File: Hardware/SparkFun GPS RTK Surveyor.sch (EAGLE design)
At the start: 98 parts, among them J2 CONN_04, J3 USB-C, J4 Qwiic Right Angle, J6 Start Base, J7 Power Switch, J9 CONN_04, Q2 MBT3904DW1T1, U1 MCP73831, U2 3.3V, U3 ZED-F9P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

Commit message: Production of v10
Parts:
- removed D9: BLUE, SparkFun-LED:LED-BLUE0603
- removed JP9: JUMPER-SMT_3_2-NC_TRACE_SILK, SparkFun-Jumpers:JUMPER-SMT_3_2-NC_TRACE_SILK
- removed R13: 1k, SparkFun-Resistors:1KOHM-0603-1/10W-1%
- removed R18, R19, R6: 33, SparkFun-Resistors:33OHM-0603-1/10W-1%
- removed R21, R22: 2.2k, SparkFun-Resistors:2.2KOHM-0603-1/10W-1%
- added C14: 10uF, SparkFun-Capacitors:10UF-0603-6.3V-20%
- added J11, J12, J13, J14: (no value), SparkFun-Connectors:CONN_041X04_NO_SILK_NO_POP
- added J15: (no value), SparkFun-Connectors:CONN_021X02_NO_SILK
- J1: device SparkFun-Connectors:CONN_08NO_SILK_DNP -> SparkFun-Connectors:CONN_041X04_NO_SILK_NO_POP
- R4: device SparkFun-Resistors:33OHM-0603-1/10W-1% -> SparkFun-Resistors:33OHM_RA-1206-1/16W-5%
- S1, S4: device SparkFun-Switches:MOMENTARY-SWITCH-SPST-SMD-6.0X3.5MM -> SparkFun-Switches:MOMENTARY-SWITCH-SPST-SMD-5.2-TALL-REDUNDANT
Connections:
- removed net !RESET: J1.6, R2D.2
- removed net !SAFE: J1.7, R2C.2
- removed net ATMEGA328_D10: R26.1
- removed net ATMEGA328_D13_SCK: R34.1
- removed net ATMEGA328_D2: J6.2
- removed net ATMEGA328_D6: R24.1
- removed net ATMEGA328_D9: R25.1
- removed net ESP32_IO12_MISO1: U5.MISO_H/IO12
- removed net ESP32_IO13_MOSI1: U5.MOSI_H/IO13
- removed net ESP32_IO15: U5.CS0_H/IO15
- removed net ESP32_IO2: U5.IO2
- removed net ESP32_IO4: U5.IO4
- removed net ESP32_IO5: R10.2, U5.CS0_V/IO5
- removed net EXTERNAL_SERIAL2_RXI: J9.3
- removed net EXTERNAL_SERIAL2_TXO: J9.2
- removed net N$14: R6.1, U3.RX2
- removed net N$19: R18.1, U3.RTK_STAT
- removed net N$20: R19.1, U3.GEO_STAT
- removed net N$23: D9.A, R10.1
- removed net N$7: D4.A, R13.1
- removed net SCL_PU1: JP9.1, R21.2
- removed net SDA_PU1: JP9.3, R22.2
- removed net SHLD: J3.SHLD
- removed net TX2_P: R4.1, U3.TX2
- new net !SAFE!: J13.2, R2C.2
- new net ESP32_12/BLUETOOTH_STATUS: R10.1, U5.MISO_H/IO12
- new net ESP32_13/POSACC1: R24.1, U5.MOSI_H/IO13
- new net ESP32_15/POSACC2: R25.1, U5.CS0_H/IO15
- new net ESP32_2/POSACC3: R26.1, U5.IO2
- new net ESP32_4/BASE_STAT: R34.1, U5.IO4
- new net ESP32_5/BASE_SELECT: J6.2, U5.CS0_V/IO5
- new net FENCE_LV: R4A.2, U3.GEO_STAT
- new net N$3: D4.A, R10.2
- new net RTK_LV: R4B.2, U3.RTK_STAT
- new net RX2_LV: R4C.2, U3.RX2
- new net TX2_LV: R4D.2, U3.TX2
- new net ZED_!RESET!: J13.3, R2D.2
- net 3.3V: now also C14.1, J1.4, J12.4, R12.2; no longer J1.1, JP9.2
- net 5V: now also J11.4, J7.2; no longer J7.1
- net ESP32_I34: now also J14.2
- net ESP32_I35: now also J14.1
- net ESP32_IO21_SDA: no longer R22.1
- net ESP32_IO22_SCL: no longer R21.1
- net ESP32_IO32: now also J14.4
- net ESP32_IO33: now also J14.3
- net EXTERNAL_SERIAL1_RXI: now also J12.2
- net EXTERNAL_SERIAL1_TXO: now also J12.3
- net FENCE_STAT: now also J1.2, R4A.1; no longer J1.5, R13.2, R19.2
- net GND: now also C14.2, J1.1, J11.1, J12.1, J3.SHLD; no longer D3.C, D9.C, J1.8
- net PPS_STAT: now also J13.1; no longer J1.3
- net RTK_STAT: now also D3.C, J1.3, R4B.1; no longer J1.4, R12.2, R18.2
- net TX_READY: now also J13.4; no longer J1.2
- net VBATT_SWTICHED: now also J7.1; no longer J7.2
- net ZED-RXI1: now also J15.2
- net ZED-RXI2: now also J11.2, J9.3, R4C.1; no longer R6.2
- net ZED-TXO1: now also J15.1
- net ZED-TXO2: now also J11.3, J9.2, R4D.1; no longer R4.2
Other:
- note added: "Bluetooth Status"
- note added: "Close DUAL_OUTPUT jumper to output NMEA Serial1 to both Bluetooth and external Serial1 port."
- note added: "RTK Solution: Off: None Blinking: Float Solid: Fixed"
- note added: "≤1000mm"
- note added: "≤100mm"
- note added: "≤20mm"
- note removed: "14.1mm RTK fix horz accuracy So no 1cm LED"
- note removed: "<100cm"
- note removed: "<10cm"
- note removed: "<1cm"
- note removed: "Close DUAL_OUTPUT jumper to output NMEA Serial1 to both Bluetooth and external Serial1 port. Warning: Jumper must be open if SERIAL1_CONNECTION is set to EXT CNTR and BLUETOOTH_BROADCAST is set to"
- note removed: "Flashing RTK at 2Hz is RTK Float Fix"
- note removed: "I2C Pull Ups"
- note removed: "Invert RTK LED"
- note removed: "PTH holes to a few GPIO on ATmega"
- note removed: "PTH holes to all primary signals (RX/TX1, RX/TX2, etc)"
- note removed: "RTK Fix: RTK LED turns off SW Map Icon turns green RTK Fix"
- moved on the sheet: BLUETOOTH_BROADCAST, BYP, C10, C11, C12, C13, C8, C9, D10, D11, D12, D15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

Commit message: Completed 4 layer design with 4pin SMD JST connectors
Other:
- note added: "Data Output Selection"
- note added: "RTK Solution: Off: None Blinking: Float On: Fixed"
- note added: "add microSD"
- note removed: "RTK Solution: Off: None Blinking: Float Solid: Fixed"
- moved on the sheet: BLUETOOTH_BROADCAST, BYP, C13, C14, C8, C9, D1, D15, D3, D5, D7, DUAL_OUTPUT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

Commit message: v11 add microSD. Fix power switch. Fix BT switch. Add I2C. Remove old files. Add enclsoure cut files.
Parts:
- removed BYP: JUMPER-SMT_2_NO_SILK, SparkFun-Jumpers:JUMPER-SMT_2_NO_SILK
- removed D15: Yellow, SparkFun-LED:LED-YELLOW0603
- removed F1: 6V/2A, SparkFun-Fuses:PPTC_6V2A
- removed LED1: GREEN, SparkFun-LED:LED-GREEN0603
- removed R33: 1k, SparkFun-Resistors:1KOHM-0603-1/10W-1%
- removed R36: 330, SparkFun-Resistors:330OHM-0603-1/10W-1%
- added C16: 0.1uF, SparkFun-Capacitors:0.1UF-0603-25V-(+80/-20%)
- added D9: 3A/10V/280mV, SparkFun-DiscreteSemi:DIODE-SCHOTTKY-BAT60A
- added J17: MICRO-SD, SparkFun-Connectors:MICRO-SD_CARD_SOCKETPUSH-PUSH
- added R13: 100k, SparkFun-Resistors:100KOHM-0603-1/10W-1%
- D10, D11, D8: value BLUE -> GREEN; device SparkFun-LED:LED-BLUE0603 -> SparkFun-LED:LED-GREEN0603
- D12: value BLUE -> RED; device SparkFun-LED:LED-BLUE0603 -> SparkFun-LED:LED-RED0603
- D3: value GREEN -> WHITE; device SparkFun-LED:LED-GREEN0603 -> SparkFun-LED:LED-WHITE0603
- R7: value 2.2k -> 1k; device SparkFun-Resistors:2.2KOHM-0603-1/10W-1% -> SparkFun-Resistors:1KOHM-0603-1/10W-1%
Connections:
- net ESP32_13/POSACC1 renamed ESP32_13/POSACC3
- net ESP32_2/POSACC3 renamed ESP32_2/POSACC1
- removed net ESP32_IO21_SDA: U5.IO21
- removed net ESP32_IO22_SCL: U5.IO22
- removed net ESP32_IO25: U5.IO25
- removed net ESP32_IO26: U5.IO26
- removed net ESP32_IO27: U5.IO27
- removed net N$28: LED1.A, R36.1
- removed net N$31: D15.A, R33.1
- removed net TX_READY: J13.4, R9A.2
- removed net VBATT_SWTICHED: D7.C, J7.1
- removed net ZED_!RESET!: J13.3, R2D.2
- new net ESP32_IO25/!CS!: J17.CS, R13.1, U5.IO25
- new net ESP32_IO26/TX_READY: J13.4, R9A.2, U5.IO26
- new net ESP32_IO27/ZED-!RESET!: J13.3, R2D.2, U5.IO27
- new net VIN: C9.1, D5.A, D6.5, D7.C, D9.C, J5.VBUS, J7.1, U1.VIN
- net 3.3V: now also C16.1, J17.VCC, R13.2; no longer R33.2, R36.2
- net 5V: no longer BYP.2, C9.1, D5.A, D6.5, F1.2, J5.VBUS, U1.VIN
- net ESP32_IO18_SCK0: now also J17.SCK
- net ESP32_IO19_MISO0: now also J17.DO
- net ESP32_IO23_MOSI0: now also J17.DI
- net ESP32_RXI: no longer D15.C
- net ESP32_TXO: no longer LED1.C
- net GND: now also C16.2, J17.GND, J17.SHIELD
- net N$32: now also D9.A; no longer BYP.1, F1.1
- net SCL: now also U5.IO22
- net SDA: now also U5.IO21
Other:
- note added: "5V is not guaranteed May be 3.5-5V"
- note added: "Charge current: 1000mA (1000V/Rprog)"
- note added: "USB-to-Serial For ESP32"
- note added: "μSD"
- note removed: "Charge current: 450mA (1000V/Rprog)"
- note removed: "This is the bypass jumper Close only if you know what you're doing."
- note removed: "USB-to-Serial"
- note removed: "add microSD"
- moved on the sheet: C4, C5, C6, C8, C9, D5, D6, D7, J10, J13, J15, J5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

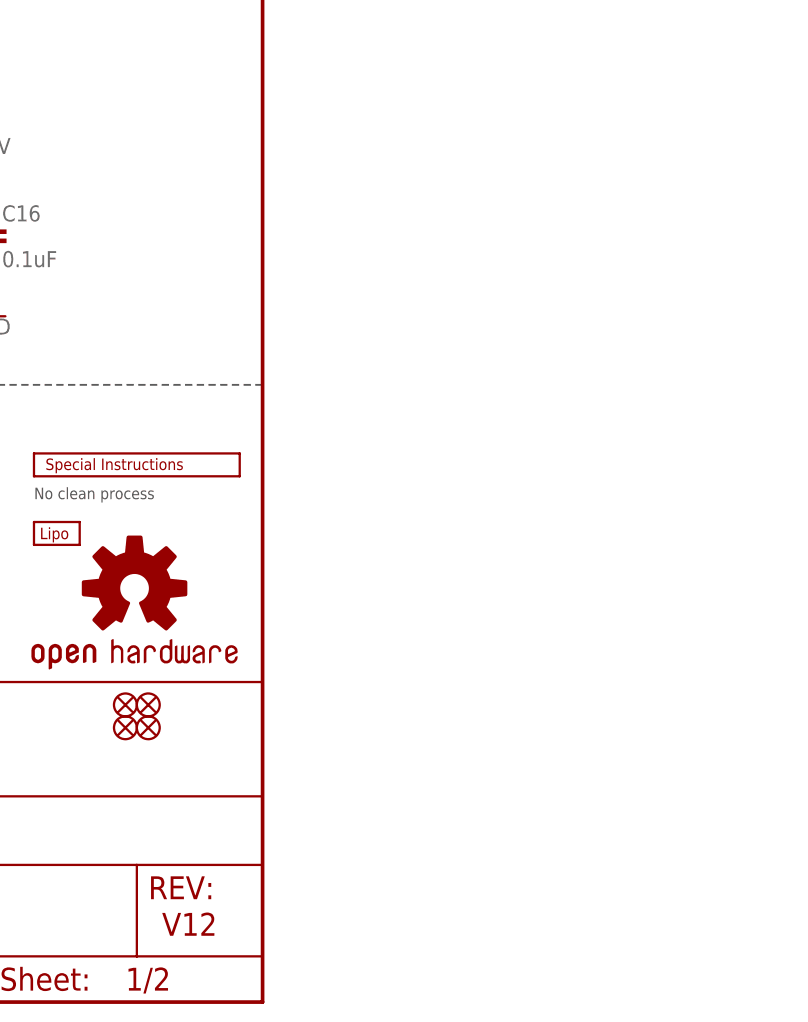
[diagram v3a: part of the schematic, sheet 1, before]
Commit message: Change LED colors.
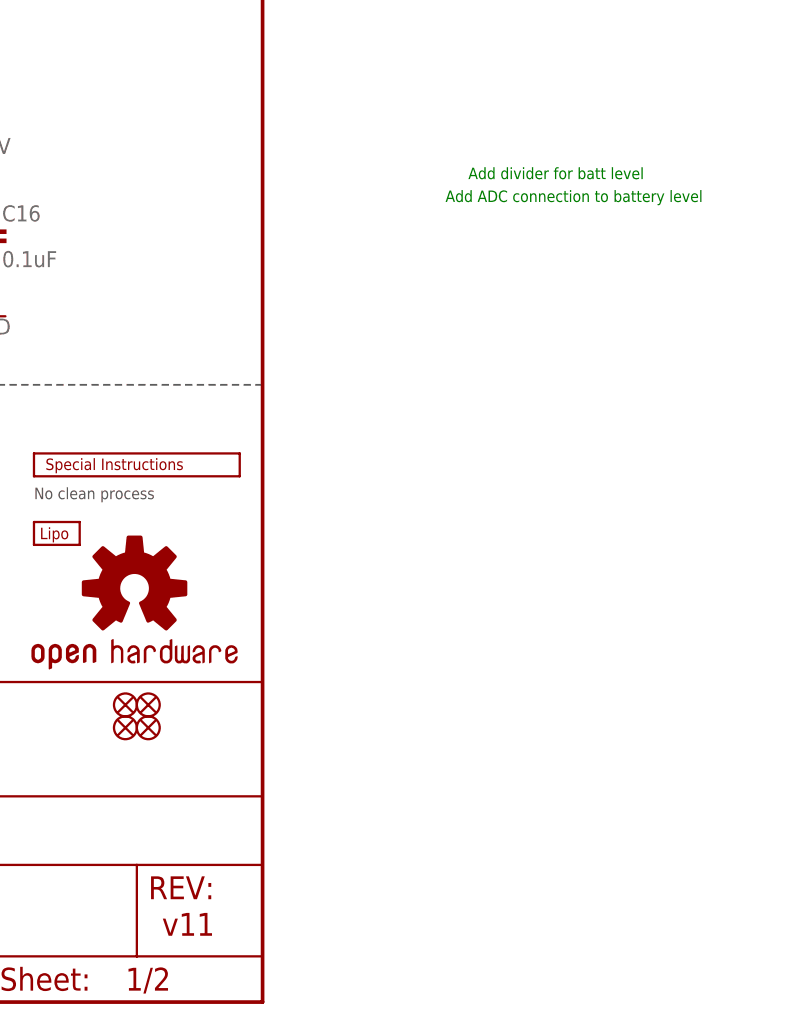
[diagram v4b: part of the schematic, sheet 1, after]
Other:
- note added: "Add ADC connection to battery level"
- note added: "Add divider for batt level"
- note added: "v11"
- note removed: "V12"
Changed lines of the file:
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@@
 <?xml version="1.0" encoding="utf-8"?>
 <!DOCTYPE eagle SYSTEM "eagle.dtd">
-<eagle version="9.6.0">
+<eagle version="9.6.2">
 <drawing>
 <settings>
@@
 <sheet>
 <plain>
-<text x="420.624" y="7.366" size="2.54" layer="94">V12</text>
+<text x="420.624" y="7.366" size="2.54" layer="94">v11</text>
 <text x="93.98" y="187.96" size="1.778" layer="97" align="center">7-bit unshifted I2C address: 0x42</text>
 <text x="89.662" y="262.382" size="2.54" layer="94" rot="MR180" align="center">Ublox ZED-F9P</text>
@@
 <text x="104.14" y="30.48" size="1.27" layer="97" align="center">5V is not guaranteed
 May be 3.5-5V</text>
+<text x="454.66" y="91.44" size="1.27" layer="91">Add divider for batt level</text>
+<text x="452.12" y="88.9" size="1.27" layer="91">Add ADC connection to battery level</text>
 </plain>
 <instances>

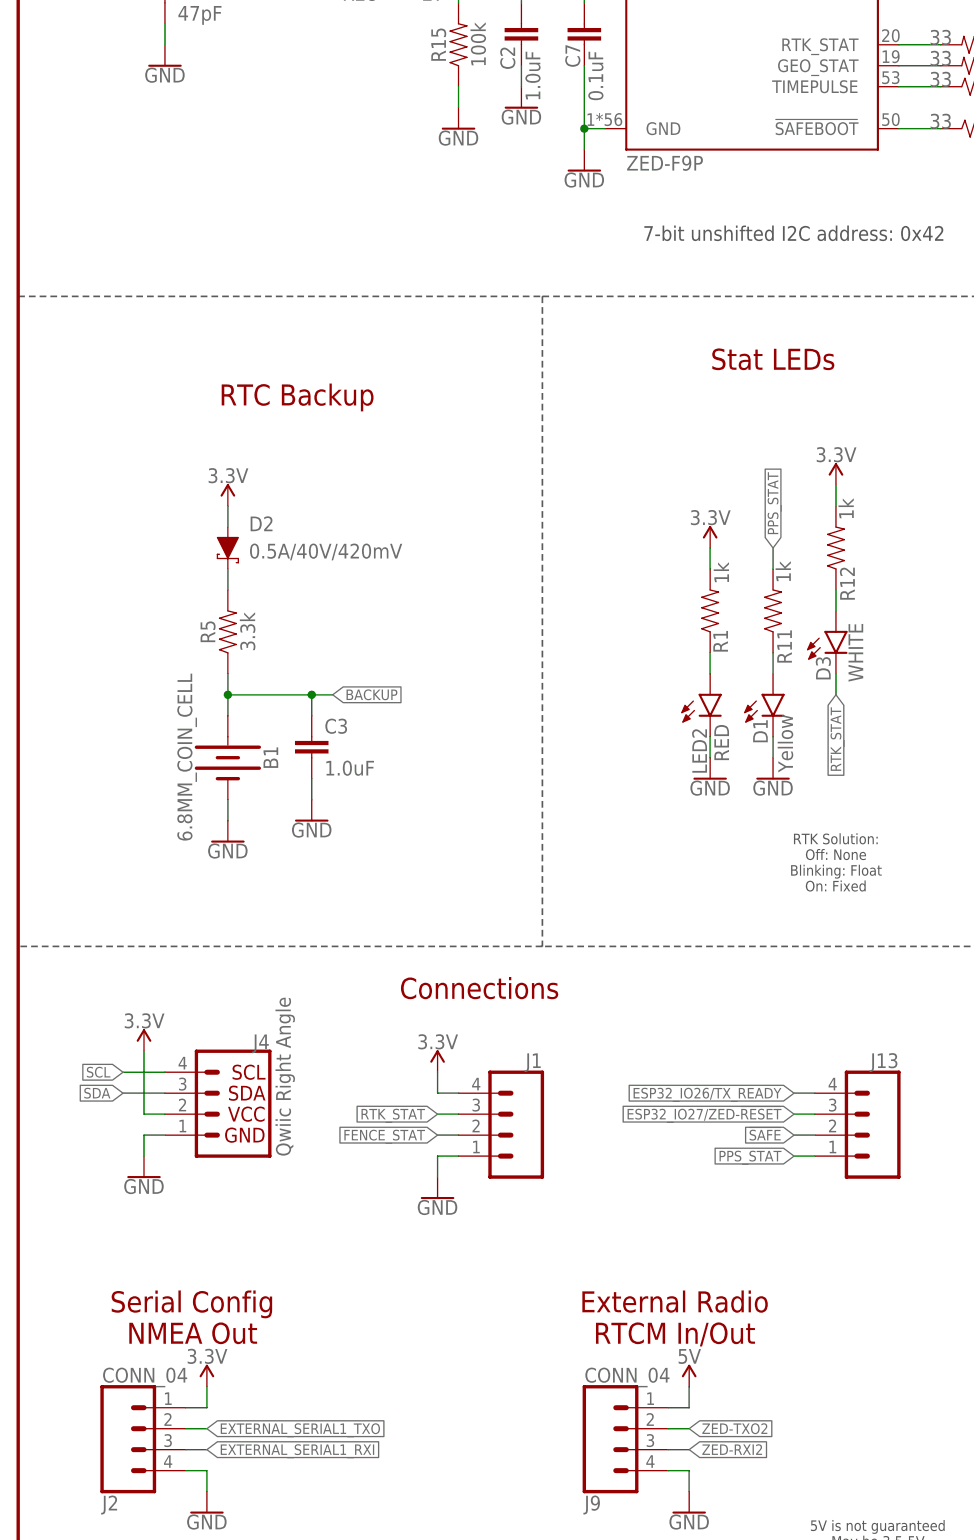
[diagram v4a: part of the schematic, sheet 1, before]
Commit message: Update parts with prod_ids
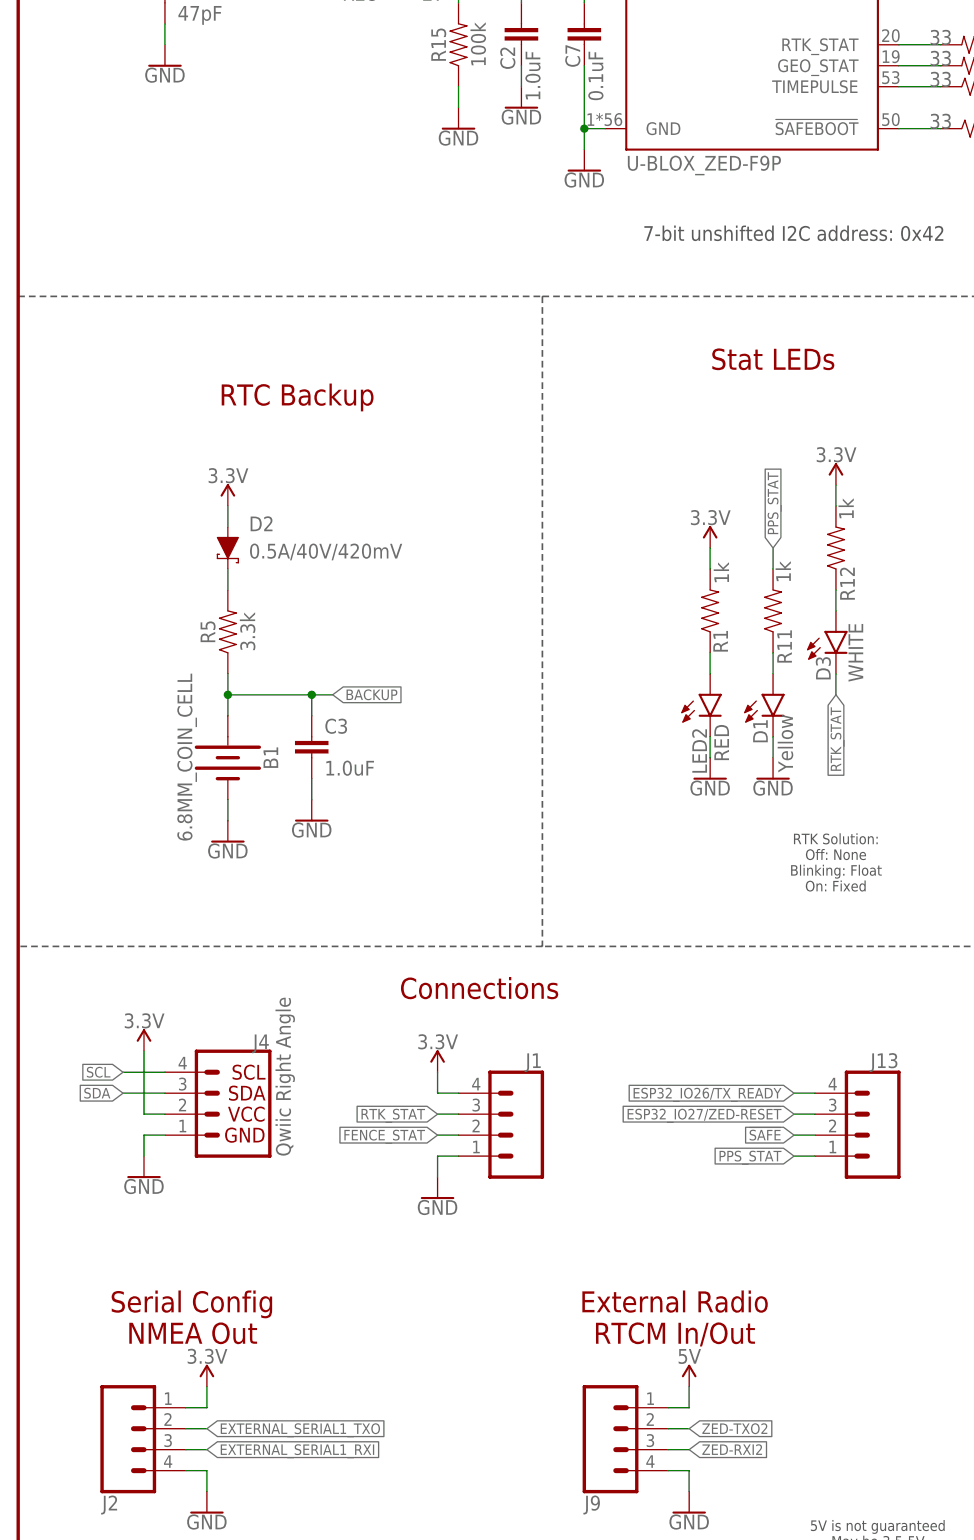
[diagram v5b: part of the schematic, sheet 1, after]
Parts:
- J2, J9: value CONN_04 -> (none); device SparkFun GPS RTK Surveyor:CONN_04 -> SparkFun-Connectors:CONN_04JST-SMD-LOCKING
- JP21, JP61, JP71, JP81: device SparkFun:FIDUCIALUFIDUCIAL -> SparkFun-Aesthetics:FIDUCIALUFIDUCIAL
- U3: value ZED-F9P -> U-BLOX_ZED-F9P; device ZED-F9P:ZED-F9P -> SparkFun-GPS:U-BLOX_ZED-F9P
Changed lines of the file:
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@@
 <?xml version="1.0" encoding="utf-8"?>
 <!DOCTYPE eagle SYSTEM "eagle.dtd">
-<eagle version="9.6.2">
+<eagle version="9.5.2">
 <drawing>
 <settings>
@@
 </classes>
 <parts>
-<part name="JP21" library="SparkFun" deviceset="FIDUCIAL" device="UFIDUCIAL"/>
-<part name="JP61" library="SparkFun" deviceset="FIDUCIAL" device="UFIDUCIAL"/>
+<part name="JP21" library="SparkFun-Aesthetics" deviceset="FIDUCIAL" device="UFIDUCIAL" value="FIDUCIALUFIDUCIAL"/>
+<part name="JP61" library="SparkFun-Aesthetics" deviceset="FIDUCIAL" device="UFIDUCIAL" value="FIDUCIALUFIDUCIAL"/>
 <part name="SUPPLY8" library="SparkFun-PowerSymbols" deviceset="3.3V" device=""/>
 <part name="J4" library="SparkFun-Connectors" deviceset="I2C_STANDARD" device="QWIIC" value="Qwiic Right Angle"/>
@@
 <part name="R5" library="SparkFun-Resistors" deviceset="3.3KOHM" device="-0603-1/10W-1%" value="3.3k"/>
 <part name="R11" library="SparkFun-Resistors" deviceset="1KOHM" device="-0603-1/10W-1%" value="1k"/>
-<part name="JP71" library="SparkFun" deviceset="FIDUCIAL" device="UFIDUCIAL"/>
-<part name="JP81" library="SparkFun" deviceset="FIDUCIAL" device="UFIDUCIAL"/>
+<part name="JP71" library="SparkFun-Aesthetics" deviceset="FIDUCIAL" device="UFIDUCIAL" value="FIDUCIALUFIDUCIAL"/>
+<part name="JP81" library="SparkFun-Aesthetics" deviceset="FIDUCIAL" device="UFIDUCIAL" value="FIDUCIALUFIDUCIAL"/>
 <part name="SUPPLY1" library="SparkFun-PowerSymbols" deviceset="3.3V" device=""/>
 <part name="GND27" library="SparkFun-PowerSymbols" deviceset="GND" device=""/>
@@
 <part name="FB1" library="SparkFun-Coils" deviceset="FERRITE_BEAD" device="-0402-2.66OHM-1GHZ" value="2.66Ω"/>
 <part name="LOGO2" library="SparkFun-Aesthetics" deviceset="SFE_LOGO_NAME_FLAME" device=".1_INCH"/>
-<part name="U3" library="ZED-F9P" deviceset="ZED-F9P" device=""/>
+<part name="U3" library="SparkFun-GPS" deviceset="U-BLOX_ZED-F9P" device=""/>
 <part name="R16" library="SparkFun-Resistors" deviceset="5.1KOHM" device="5.1KOHM-0603-1/10W-1%" value="5.1k"/>
 <part name="R17" library="SparkFun-Resistors" deviceset="5.1KOHM" device="5.1KOHM-0603-1/10W-1%" value="5.1k"/>
@@
 <part name="GND43" library="SparkFun-PowerSymbols" deviceset="GND" device=""/>
 <part name="SUPPLY22" library="SparkFun-PowerSymbols" deviceset="3.3V" device=""/>
-<part name="J9" library="SparkFun GPS RTK Surveyor" deviceset="CONN_04" device=""/>
+<part name="J9" library="SparkFun-Connectors" deviceset="CONN_04" device="JST-SMD-LOCKING"/>
 <part name="SUPPLY18" library="SparkFun-PowerSymbols" deviceset="5V" device=""/>
-<part name="J2" library="SparkFun GPS RTK Surveyor" deviceset="CONN_04" device=""/>
+<part name="J2" library="SparkFun-Connectors" deviceset="CONN_04" device="JST-SMD-LOCKING"/>
 <part name="P+2" library="SparkFun-PowerSymbols" deviceset="3.3V" device=""/>
 <part name="R10" library="SparkFun-Resistors" deviceset="1KOHM" device="-0603-1/10W-1%" value="1k"/>
